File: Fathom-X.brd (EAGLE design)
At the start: 63.5 x 45.7 mm, 31 parts, among them IC1 1117-3.3V

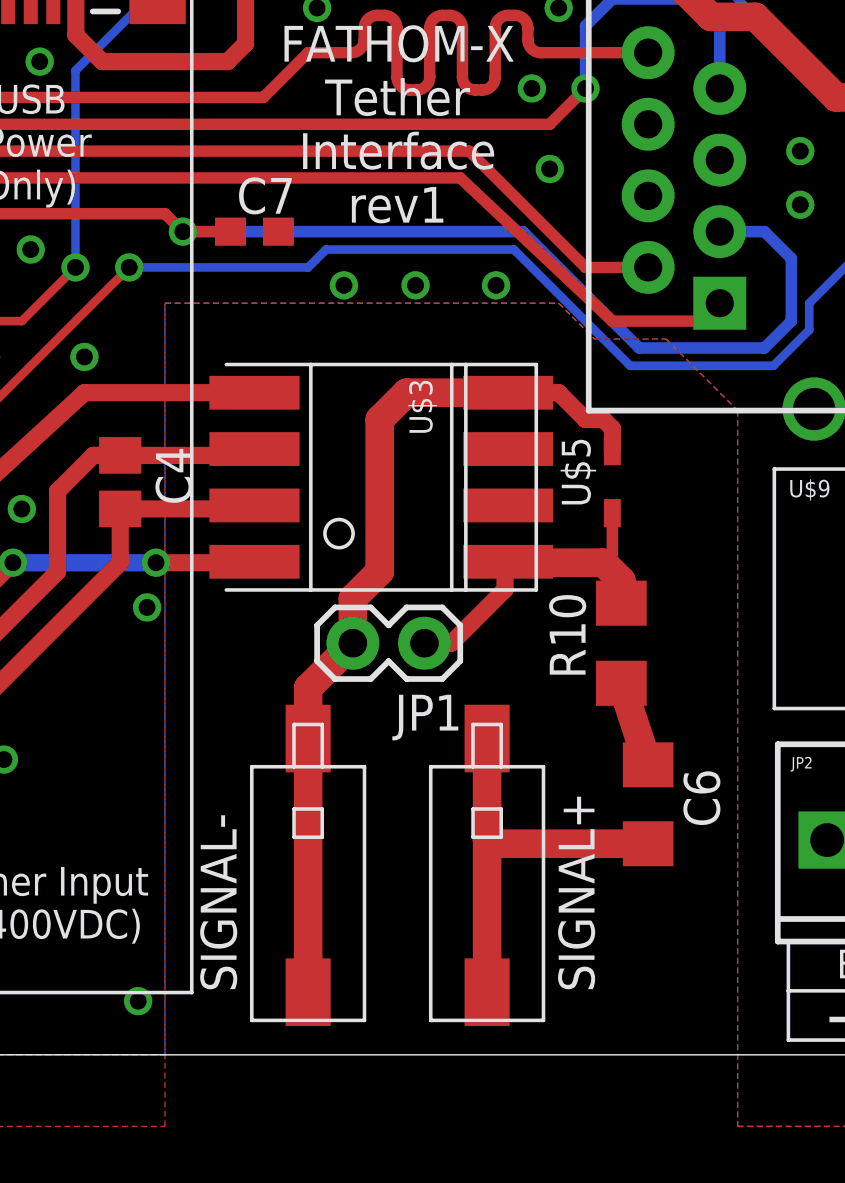
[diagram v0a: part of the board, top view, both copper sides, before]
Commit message: Fathom-X: Update signal connector
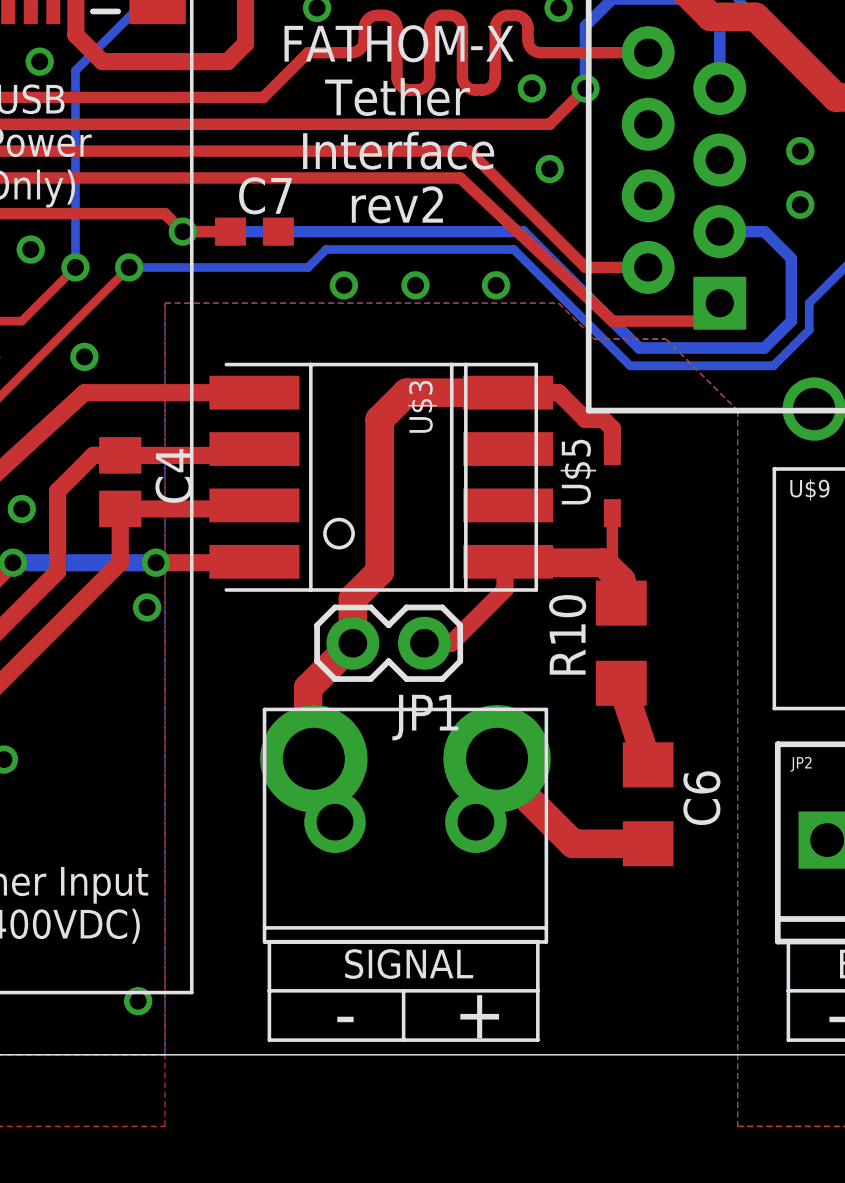
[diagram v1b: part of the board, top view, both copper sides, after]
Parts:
- removed U$2, U$4: HEADER-1NQ, BlueRobotics-Main:NQ0121X000J0G
- added U$8: HEADER-2POWER, BlueRobotics-Main:TETHER-POWER-TERMINALS
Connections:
- net HV_SIGNAL: now also U$8.2A, U$8.2B; no longer U$2.P$1, U$2.P$2
- net PL_L: now also U$8.1A, U$8.1B; no longer U$4.P$1, U$4.P$2
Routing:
- net HV_SIGNAL: track 14.8 -> 9.24 mm
- net PL_L: track 31.6 -> 26.7 mm
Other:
- board text added: "FATHOM-X Tether Interface rev2"
- board text added: "SIGNAL"
- board text removed: "FATHOM-X Tether Interface rev1"
- board text removed: "SIGNAL+"
- board text removed: "SIGNAL-"
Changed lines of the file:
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@@
 <text x="1.5875" y="23.8125" size="1.27" layer="21" ratio="12">PWR</text>
 <text x="1.27" y="14.9225" size="1.27" layer="21" ratio="12">LINK</text>
-<text x="30.48" y="2.2225" size="1.27" layer="21" ratio="12" rot="R90">SIGNAL-</text>
-<text x="43.18" y="2.2225" size="1.27" layer="21" ratio="12" rot="R90">SIGNAL+</text>
 <text x="36.195" y="33.02" size="1.27" layer="21" ratio="12" align="center">FATHOM-X
 Tether
 Interface
-rev1</text>
+rev2</text>
 <text x="23.1775" y="32.385" size="1.016" layer="21" ratio="12" rot="R180" align="center">USB
 (Power
@@
 <text x="16.1925" y="0.9525" size="1.016" layer="22" rot="MR0">R.J. 2016/02</text>
 <text x="52.3875" y="40.005" size="1.016" layer="21" ratio="12">10/100</text>
+<wire x1="31.645" y1="4.01625" x2="41.17" y2="4.01625" width="0.127" layer="21"/>
+<wire x1="41.17" y1="4.01625" x2="41.17" y2="2.27" width="0.127" layer="21"/>
+<wire x1="41.17" y1="2.27" x2="41.17" y2="0.52375" width="0.127" layer="21"/>
+<wire x1="41.17" y1="0.52375" x2="36.4075" y2="0.52375" width="0.127" layer="21"/>
+<wire x1="36.4075" y1="0.52375" x2="31.645" y2="0.52375" width="0.127" layer="21"/>
+<wire x1="31.645" y1="0.52375" x2="31.645" y2="2.27" width="0.127" layer="21"/>
+<text x="36.56625" y="3.2225" size="1.016" layer="21" font="fixed" ratio="12" align="center">SIGNAL</text>
+<wire x1="31.645" y1="2.27" x2="31.645" y2="4.01625" width="0.127" layer="21"/>
+<wire x1="31.645" y1="2.27" x2="36.4075" y2="2.27" width="0.127" layer="21"/>
+<wire x1="36.4075" y1="2.27" x2="41.17" y2="2.27" width="0.127" layer="21"/>
+<wire x1="36.4075" y1="2.27" x2="36.4075" y2="0.52375" width="0.127" layer="21"/>
+<text x="39.10625" y="1.47625" size="1.778" layer="21" font="fixed" ratio="12" align="center">+</text>
+<text x="34.34375" y="1.47625" size="1.778" layer="21" font="fixed" ratio="12" align="center">-</text>
 </plain>
 <attributes>
@@
 <element name="R9" library="resistor" package="R0603" value="470" x="14.605" y="26.035" rot="R180"/>
 <element name="R11" library="resistor" package="R0603" value="470" x="14.605" y="22.86" rot="R180"/>
-<element name="U$2" library="BlueRobotics-Main" package="NQ0121X000J0G" value="HEADER-1NQ" x="39.37" y="2.2225"/>
-<element name="U$4" library="BlueRobotics-Main" package="NQ0121X000J0G" value="HEADER-1NQ" x="33.02" y="2.2225"/>
 <element name="JP2" library="SparkFun-Connectors" package="SCREWTERMINAL-3.5MM-2" value="M023.5MM" x="51.435" y="7.62"/>
 <element name="JP1" library="SparkFun-Connectors" package="1X02" value="M02PTH" x="37.1475" y="14.605" rot="R180"/>
@@
 <element name="C1" library="SparkFun-Passives" package="EIA3216" value="10uF 10V" x="45.085" y="43.18" rot="R180"/>
 <element name="IC1" library="BlueRobotics-Main" package="SOT223" value="1117-3.3V" x="37.1475" y="40.9575" rot="R90"/>
+<element name="U$8" library="BlueRobotics-Main" package="TETHER-POWER-TERMINALS" value="HEADER-2POWER" x="33.9725" y="8.255"/>
 </elements>
 <signals>
@@
 <signal name="HV_SIGNAL">
 <contactref element="C6" pad="2"/>
-<contactref element="U$2" pad="P$1"/>
-<contactref element="U$2" pad="P$2"/>
-<wire x1="39.37" y1="2.2225" x2="39.37" y2="7.62" width="1.016" layer="1"/>
-<wire x1="39.37" y1="7.62" x2="39.37" y2="11.2225" width="1.016" layer="1"/>
-<wire x1="45.085" y1="7.49" x2="39.5" y2="7.49" width="1.016" layer="1"/>
-<wire x1="39.5" y1="7.49" x2="39.37" y2="7.62" width="1.016" layer="1"/>
+<contactref element="U$8" pad="2B"/>
+<contactref element="U$8" pad="2A"/>
+<wire x1="45.085" y1="7.49" x2="42.42" y2="7.49" width="1.016" layer="1"/>
+<wire x1="42.42" y1="7.49" x2="40.195" y2="9.715" width="1.016" layer="1"/>
+<wire x1="40.195" y1="9.715" x2="39.7225" y2="10.505" width="1.016" layer="1"/>
+<wire x1="38.9725" y1="8.255" x2="38.655" y2="8.175" width="1.016" layer="1"/>
+<wire x1="38.655" y1="8.175" x2="40.195" y2="9.715" width="1.016" layer="1"/>
 </signal>
 <signal name="N$12">
@@
 <contactref element="U$5" pad="2"/>
 <contactref element="U$3" pad="PL_L"/>
-<contactref element="U$4" pad="P$1"/>
-<contactref element="U$4" pad="P$2"/>
 <wire x1="40.115" y1="23.495" x2="40.3225" y2="23.495" width="1.016" layer="1"/>
-<wire x1="33.02" y1="2.2225" x2="33.02" y2="11.2225" width="1.016" layer="1"/>
-<wire x1="33.02" y1="11.2225" x2="33.02" y2="13.0175" width="1.016" layer="1"/>
 <wire x1="33.02" y1="13.0175" x2="34.6075" y2="14.605" width="1.016" layer="1"/>
 <wire x1="34.6075" y1="14.605" x2="34.6075" y2="16.1925" width="1.016" layer="1"/>
@@
 <wire x1="42.8625" y1="22.5425" x2="41.91" y2="23.495" width="0.6096" layer="1"/>
 <wire x1="41.91" y1="23.495" x2="40.115" y2="23.495" width="0.6096" layer="1"/>
+<contactref element="U$8" pad="1A"/>
+<contactref element="U$8" pad="1B"/>
+<wire x1="33.02" y1="13.0175" x2="33.02" y2="9.985" width="1.016" layer="1"/>
+<wire x1="33.02" y1="9.985" x2="33.2225" y2="10.505" width="1.016" layer="1"/>
+<wire x1="33.9725" y1="8.255" x2="33.655" y2="9.12" width="1.016" layer="1"/>
+<wire x1="33.655" y1="9.12" x2="33.2225" y2="10.505" width="1.016" layer="1"/>
 </signal>
 <signal name="N$1">

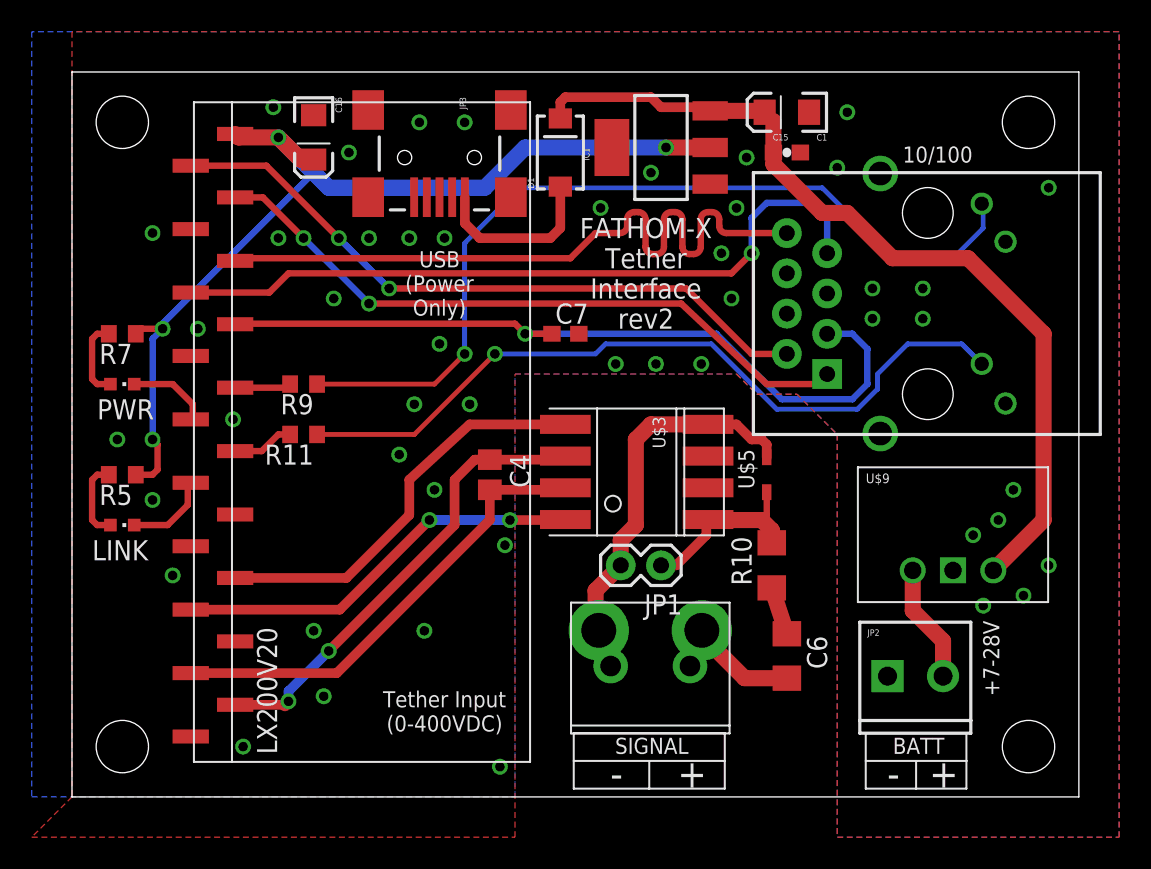
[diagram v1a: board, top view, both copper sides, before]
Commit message: Change connector.
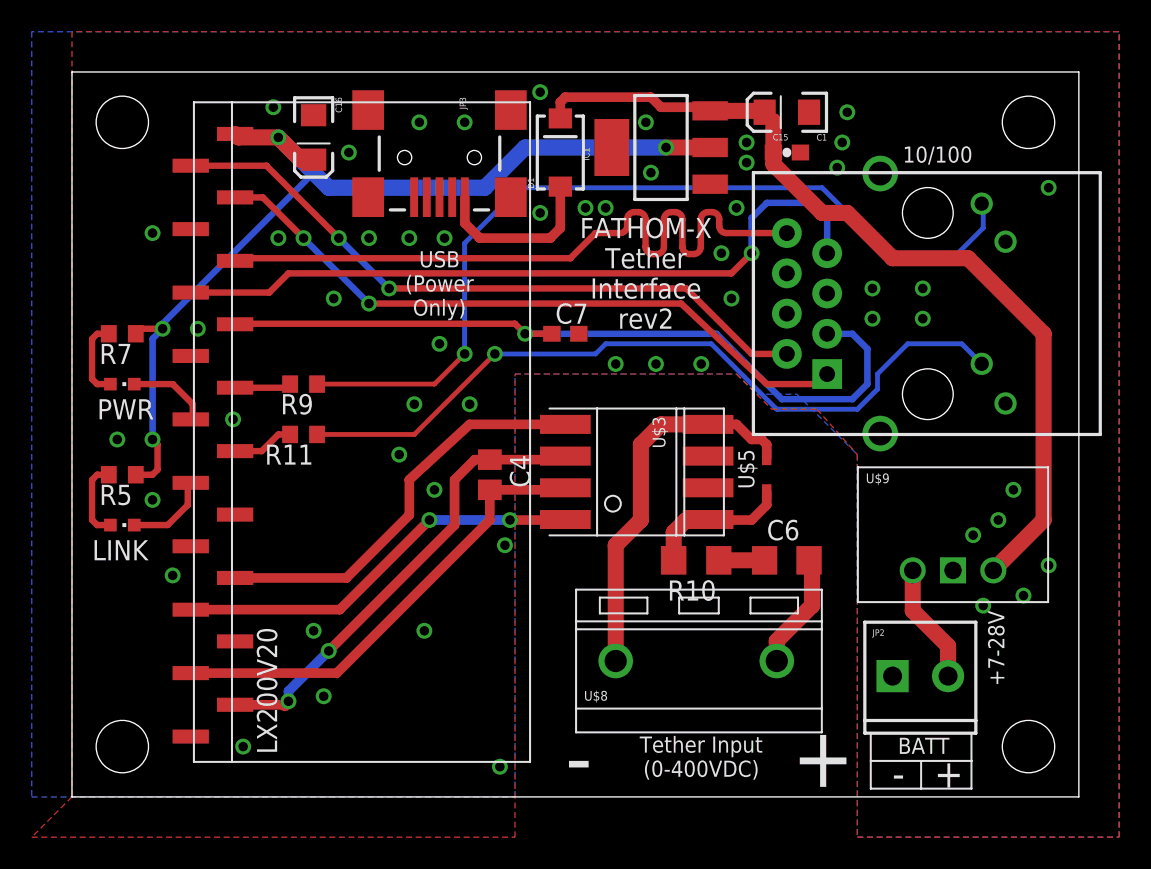
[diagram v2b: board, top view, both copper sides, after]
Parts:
- removed JP1: M02PTH, SparkFun-Connectors:1X02
- U$8: value HEADER-2POWER -> HEADER-210.16MM; device BlueRobotics-Main:TETHER-POWER-TERMINALS -> BlueRobotics-Main:HEADER-10.16MM-2POS
- moved C6 6.03 mm to (45.1, 14.9), turned to 0 degrees
- moved R10 4.77 mm to (39.4, 14.9), turned to 180 degrees
- moved U$8 0.45 mm to (34.3, 8.57)
- moved JP2 0.32 mm to (51.8, 7.62)
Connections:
- net HV_SIGNAL: now also U$8.P$2; no longer U$8.2A, U$8.2B
- net PL_L: now also U$8.P$1; no longer JP1.2, U$8.1A, U$8.1B
- net PL_N: no longer JP1.1
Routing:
- net PL_N: track 11.7 -> 9.20 mm
- net PL_L: track 26.7 -> 24.3 mm
- net HV_SIGNAL: track 9.24 -> 7.35 mm
- net GND: vias 48 -> 54
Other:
- board text added: "DANGER: POTENTIALLY HIGH VOLTAGE"
- board text added: "R.J. 2016/04"
- board text removed: "R.J. 2016/02"
- board text removed: "SIGNAL"
